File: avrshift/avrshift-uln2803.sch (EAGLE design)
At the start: 32 parts, among them IC1 AT90S2313P, IC2 7805TV

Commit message: some more minor adjustments (especially labels)
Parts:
- IC3, IC4: value (none) -> ULN2803A
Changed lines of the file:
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@@
 <part name="JP13" library="pinhead" deviceset="PINHD-1X2" device=""/>
 <part name="JP14" library="pinhead" deviceset="PINHD-1X2" device=""/>
-<part name="IC3" library="uln-udn" deviceset="ULN2803A" device=""/>
+<part name="IC3" library="uln-udn" deviceset="ULN2803A" device="" value="ULN2803A"/>
 <part name="JP2" library="pinhead" deviceset="PINHD-1X2" device=""/>
 <part name="JP3" library="pinhead" deviceset="PINHD-1X2" device=""/>
@@
 <part name="JP8" library="pinhead" deviceset="PINHD-1X2" device=""/>
 <part name="JP9" library="pinhead" deviceset="PINHD-1X2" device=""/>
-<part name="IC4" library="uln-udn" deviceset="ULN2803A" device=""/>
+<part name="IC4" library="uln-udn" deviceset="ULN2803A" device="" value="ULN2803A"/>
 </parts>
 <sheets>

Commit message: 😺
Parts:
- C2: device capacitor-wima:C2,5-3 -> rcl:C-EU050-024X044
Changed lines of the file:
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@@
 <part name="R2" library="rcl" deviceset="R-EU_" device="0207/2V" value="1K"/>
 <part name="C1" library="capacitor-wima" deviceset="C" device="2,5-3" value="330nF"/>
-<part name="C2" library="capacitor-wima" deviceset="C" device="2,5-3" value="100nF"/>
+<part name="C2" library="rcl" deviceset="C-EU" device="050-024X044" value="100nF"/>
 <part name="SJ1" library="jumper" deviceset="SJ" device="" value="BUSPWR"/>
 <part name="SV1" library="con-harting-ml" deviceset="ML10" device="" value="SI2C"/>

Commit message: avrshift-uln2803: start work on rev 2.1
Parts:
- added SV2: (no value), pinhead:PINHD-2X3
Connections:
- removed net N$3: IC1.RESET, R3.2
- new net RST: IC1.RESET, R3.1, SV2.5
- net 5V: now also R3.2, SV2.2; no longer R3.1
- net AVRO11: now also SV2.4
- net AVRO12: now also SV2.1
- net AVRO13: now also SV2.3
- net GND: now also SV2.6
- net N$10: now also R15.2; no longer R15.1
- net N$21: now also R18.1; no longer R18.2
- net N$33: now also R15.1; no longer R15.2
- net N$8: now also R18.2; no longer R18.1
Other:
- moved on the sheet: R15, R18, R3
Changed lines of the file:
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@@
 <part name="JP9" library="pinhead" deviceset="PINHD-1X2" device=""/>
 <part name="IC4" library="uln-udn" deviceset="ULN2803A" device="" value="ULN2803A"/>
+<part name="SV2" library="pinhead" deviceset="PINHD-2X3" device=""/>
 </parts>
 <sheets>
@@
 <instance part="SV1" gate="G$1" x="-53.34" y="50.8" rot="R180"/>
 <instance part="SJ2" gate="1" x="-25.4" y="71.12" rot="R270"/>
-<instance part="R3" gate="G$1" x="-38.1" y="7.62" rot="R90"/>
-<instance part="R15" gate="G$1" x="-48.26" y="17.78" rot="R90"/>
-<instance part="R18" gate="G$1" x="-58.42" y="17.78" rot="R90"/>
+<instance part="R3" gate="G$1" x="-38.1" y="7.62" rot="R270"/>
+<instance part="R15" gate="G$1" x="-48.26" y="20.32" rot="R270"/>
+<instance part="R18" gate="G$1" x="-58.42" y="20.32" rot="R270"/>
 <instance part="LED1" gate="G$1" x="-48.26" y="10.16"/>
 <instance part="LED2" gate="G$1" x="-58.42" y="10.16"/>
@@
 <instance part="JP9" gate="G$1" x="101.6" y="20.32"/>
 <instance part="IC4" gate="G$1" x="63.5" y="22.86"/>
+<instance part="SV2" gate="A" x="-12.7" y="-43.18"/>
 </instances>
 <busses>
@@
 <wire x1="45.72" y1="12.7" x2="45.72" y2="43.18" width="0.1524" layer="91"/>
 <junction x="45.72" y="43.18"/>
+</segment>
+<segment>
+<pinref part="SV2" gate="A" pin="6"/>
+<wire x1="-7.62" y1="-45.72" x2="7.62" y2="-45.72" width="0.1524" layer="91"/>
+<label x="-2.54" y="-45.72" size="1.778" layer="95"/>
 </segment>
 </net>
@@
 <segment>
 <pinref part="IC1" gate="G$1" pin="VCC"/>
+<label x="-66.04" y="0" size="1.778" layer="95"/>
 <wire x1="-30.48" y1="0" x2="-38.1" y2="0" width="0.1524" layer="91"/>
-<label x="-66.04" y="0" size="1.778" layer="95"/>
-<pinref part="R3" gate="G$1" pin="1"/>
+<pinref part="R3" gate="G$1" pin="2"/>
 <wire x1="-38.1" y1="0" x2="-68.58" y2="0" width="0.1524" layer="91"/>
 <wire x1="-38.1" y1="2.54" x2="-38.1" y2="0" width="0.1524" layer="91"/>
 <junction x="-38.1" y="0"/>
+</segment>
+<segment>
+<pinref part="SV2" gate="A" pin="2"/>
+<wire x1="-7.62" y1="-40.64" x2="7.62" y2="-40.64" width="0.1524" layer="91"/>
+<label x="-2.54" y="-40.64" size="1.778" layer="95"/>
 </segment>
 </net>
@@
 </segment>
 </net>
-<net name="N$3" class="0">
+<net name="RST" class="0">
 <segment>
 <pinref part="IC1" gate="G$1" pin="RESET"/>
 <wire x1="-30.48" y1="17.78" x2="-38.1" y2="17.78" width="0.1524" layer="91"/>
-<pinref part="R3" gate="G$1" pin="2"/>
+<pinref part="R3" gate="G$1" pin="1"/>
 <wire x1="-38.1" y1="17.78" x2="-38.1" y2="12.7" width="0.1524" layer="91"/>
 </segment>
-</net>
-<net name="N$8" class="0">
-<segment>
-<pinref part="R18" gate="G$1" pin="1"/>
-<pinref part="LED2" gate="G$1" pin="A"/>
-</segment>
-</net>
-<net name="N$10" class="0">
-<segment>
-<pinref part="R15" gate="G$1" pin="1"/>
-<pinref part="LED1" gate="G$1" pin="A"/>
+<segment>
+<pinref part="SV2" gate="A" pin="5"/>
+<wire x1="-15.24" y1="-45.72" x2="-27.94" y2="-45.72" width="0.1524" layer="91"/>
+<label x="-27.94" y="-45.72" size="1.778" layer="95"/>
 </segment>
 </net>
@@
 <wire x1="-33.02" y1="10.16" x2="-33.02" y2="27.94" width="0.1524" layer="91"/>
 <wire x1="-33.02" y1="27.94" x2="-58.42" y2="27.94" width="0.1524" layer="91"/>
-<pinref part="R18" gate="G$1" pin="2"/>
-<wire x1="-58.42" y1="27.94" x2="-58.42" y2="22.86" width="0.1524" layer="91"/>
+<pinref part="R18" gate="G$1" pin="1"/>
+<wire x1="-58.42" y1="25.4" x2="-58.42" y2="27.94" width="0.1524" layer="91"/>
 </segment>
 </net>
@@
 <wire x1="-35.56" y1="5.08" x2="-35.56" y2="25.4" width="0.1524" layer="91"/>
 <wire x1="-35.56" y1="25.4" x2="-48.26" y2="25.4" width="0.1524" layer="91"/>
-<pinref part="R15" gate="G$1" pin="2"/>
-<wire x1="-48.26" y1="25.4" x2="-48.26" y2="22.86" width="0.1524" layer="91"/>
+<pinref part="R15" gate="G$1" pin="1"/>
 </segment>
 </net>
@@
 <label x="35.56" y="53.34" size="1.778" layer="95"/>
 </segment>
+<segment>
+<pinref part="SV2" gate="A" pin="4"/>
+<wire x1="-7.62" y1="-43.18" x2="7.62" y2="-43.18" width="0.1524" layer="91"/>
+<label x="-2.54" y="-43.18" size="1.778" layer="95"/>
+</segment>
 </net>
 <net name="AVRO12" class="0">
@@
 <label x="35.56" y="55.88" size="1.778" layer="95"/>
 </segment>
+<segment>
+<pinref part="SV2" gate="A" pin="1"/>
+<wire x1="-15.24" y1="-40.64" x2="-27.94" y2="-40.64" width="0.1524" layer="91"/>
+<label x="-27.94" y="-40.64" size="1.778" layer="95"/>
+</segment>
 </net>
 <net name="AVRO13" class="0">
@@
 <wire x1="50.8" y1="58.42" x2="35.56" y2="58.42" width="0.1524" layer="91"/>
 <label x="35.56" y="58.42" size="1.778" layer="95"/>
+</segment>
+<segment>
+<pinref part="SV2" gate="A" pin="3"/>
+<wire x1="-15.24" y1="-43.18" x2="-27.94" y2="-43.18" width="0.1524" layer="91"/>
+<label x="-27.94" y="-43.18" size="1.778" layer="95"/>
 </segment>
 </net>
@@
 </segment>
 </net>
+<net name="N$8" class="0">
+<segment>
+<pinref part="R18" gate="G$1" pin="2"/>
+<pinref part="LED2" gate="G$1" pin="A"/>
+<wire x1="-58.42" y1="15.24" x2="-58.42" y2="12.7" width="0.1524" layer="91"/>
+</segment>
+</net>
+<net name="N$10" class="0">
+<segment>
+<pinref part="R15" gate="G$1" pin="2"/>
+<pinref part="LED1" gate="G$1" pin="A"/>
+<wire x1="-48.26" y1="15.24" x2="-48.26" y2="12.7" width="0.1524" layer="91"/>
+</segment>
+</net>

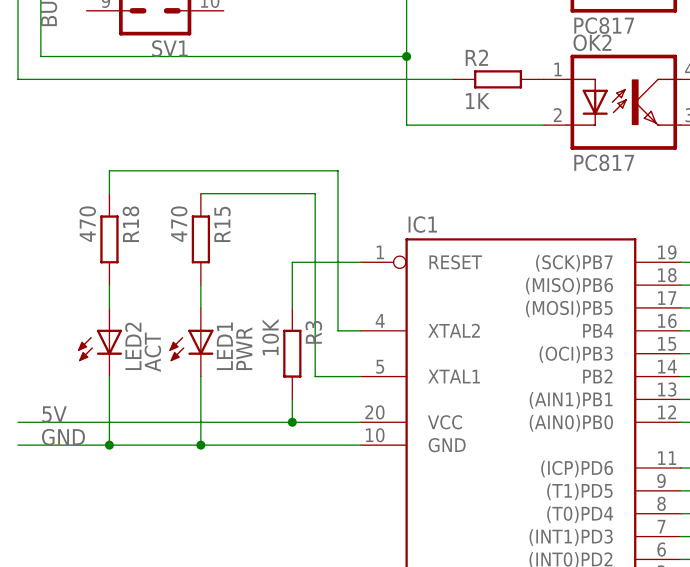
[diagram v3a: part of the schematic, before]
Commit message: avrshift: Add labels for avrmf pins, extend VCC net to 7805 and input
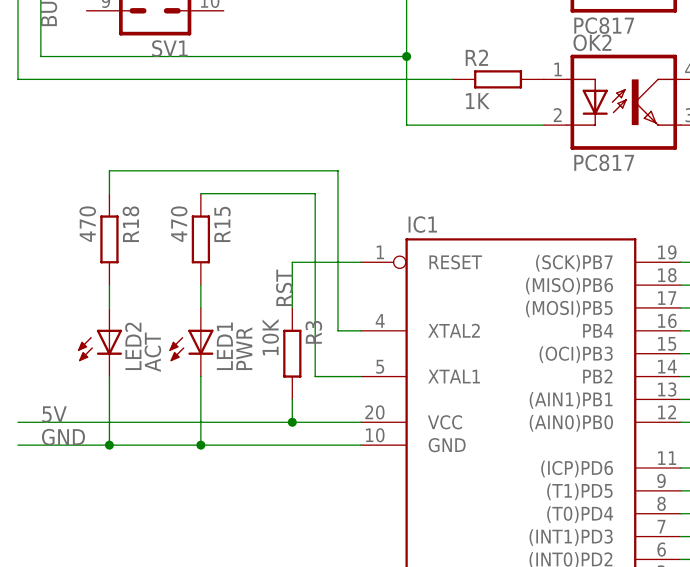
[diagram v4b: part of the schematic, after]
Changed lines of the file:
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@@
 <pinref part="R3" gate="G$1" pin="1"/>
 <wire x1="-38.1" y1="17.78" x2="-38.1" y2="12.7" width="0.1524" layer="91"/>
+<label x="-38.1" y="12.7" size="1.778" layer="95" rot="R90"/>
 </segment>
 <segment>

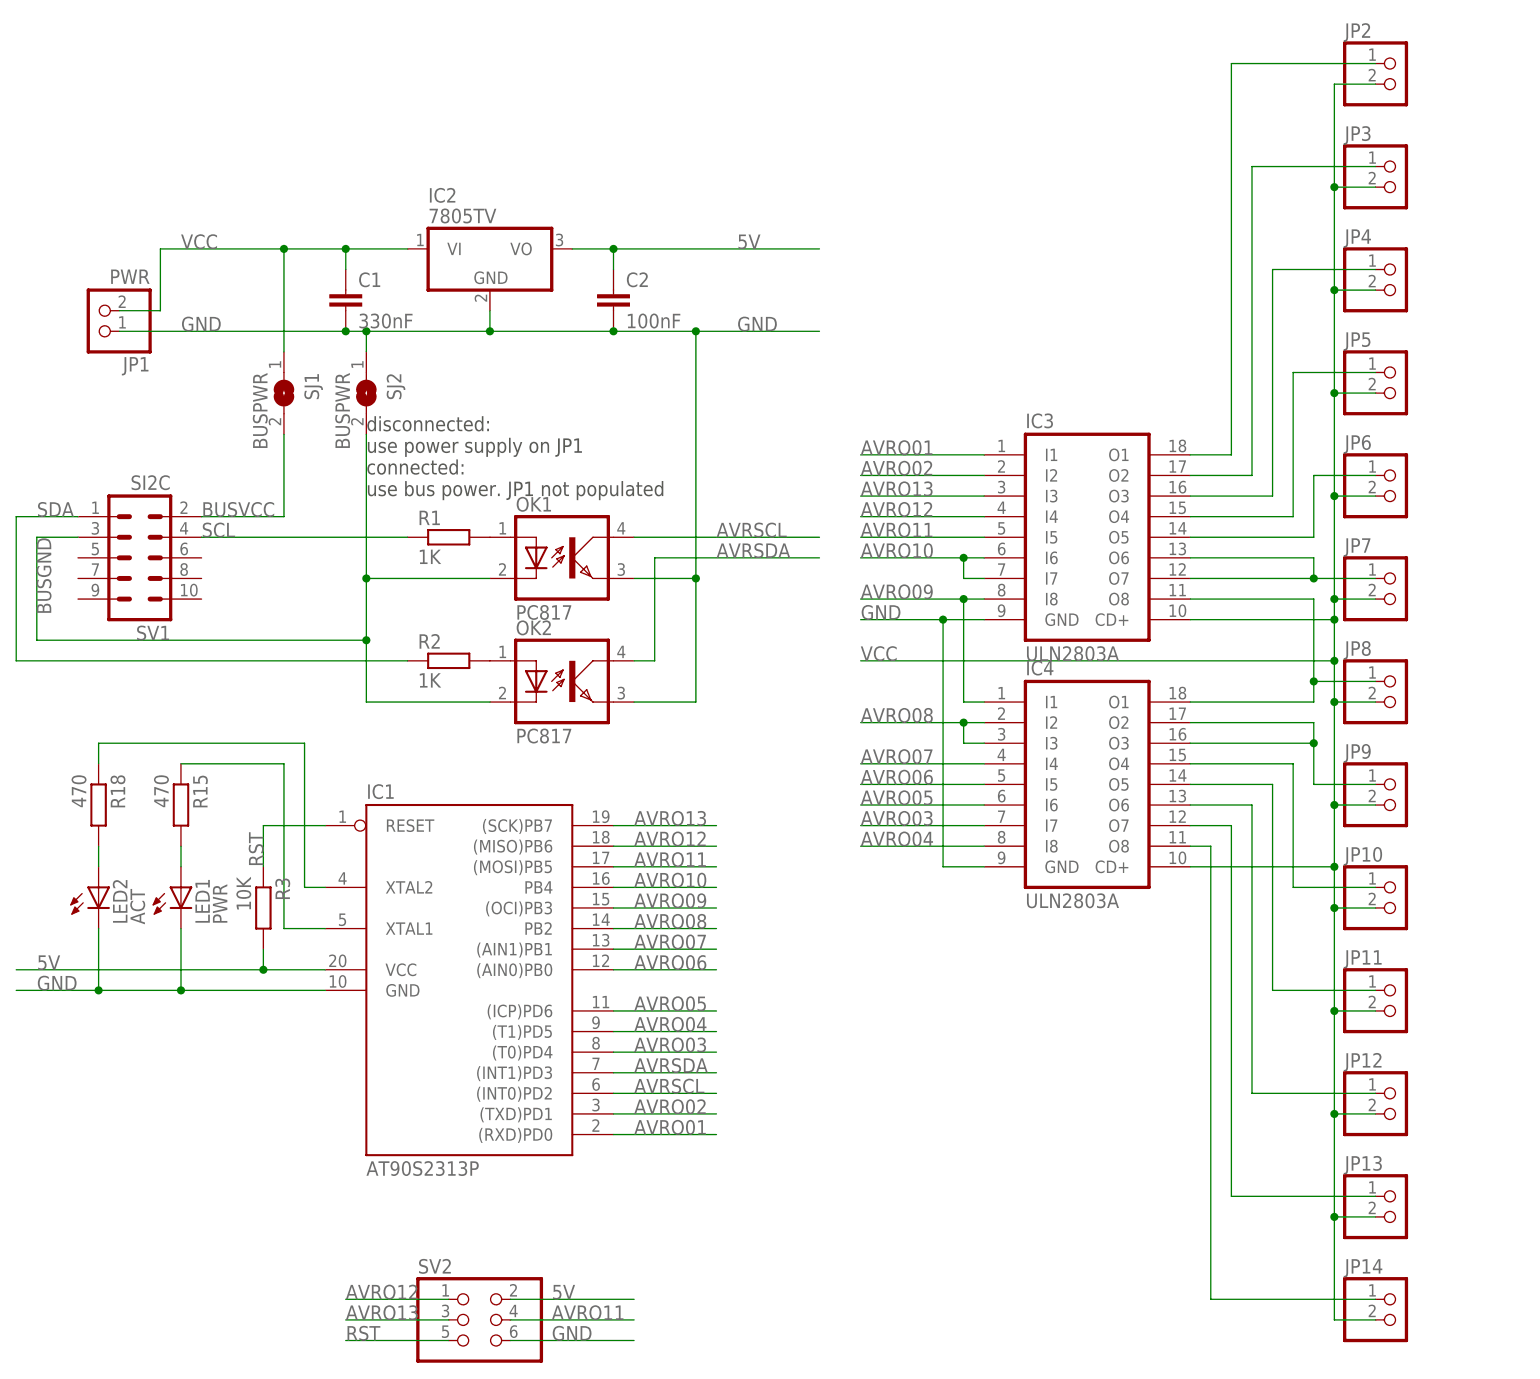
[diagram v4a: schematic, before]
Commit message: avrshift-uln2803: switch to (cheaper) SMD ATTiny
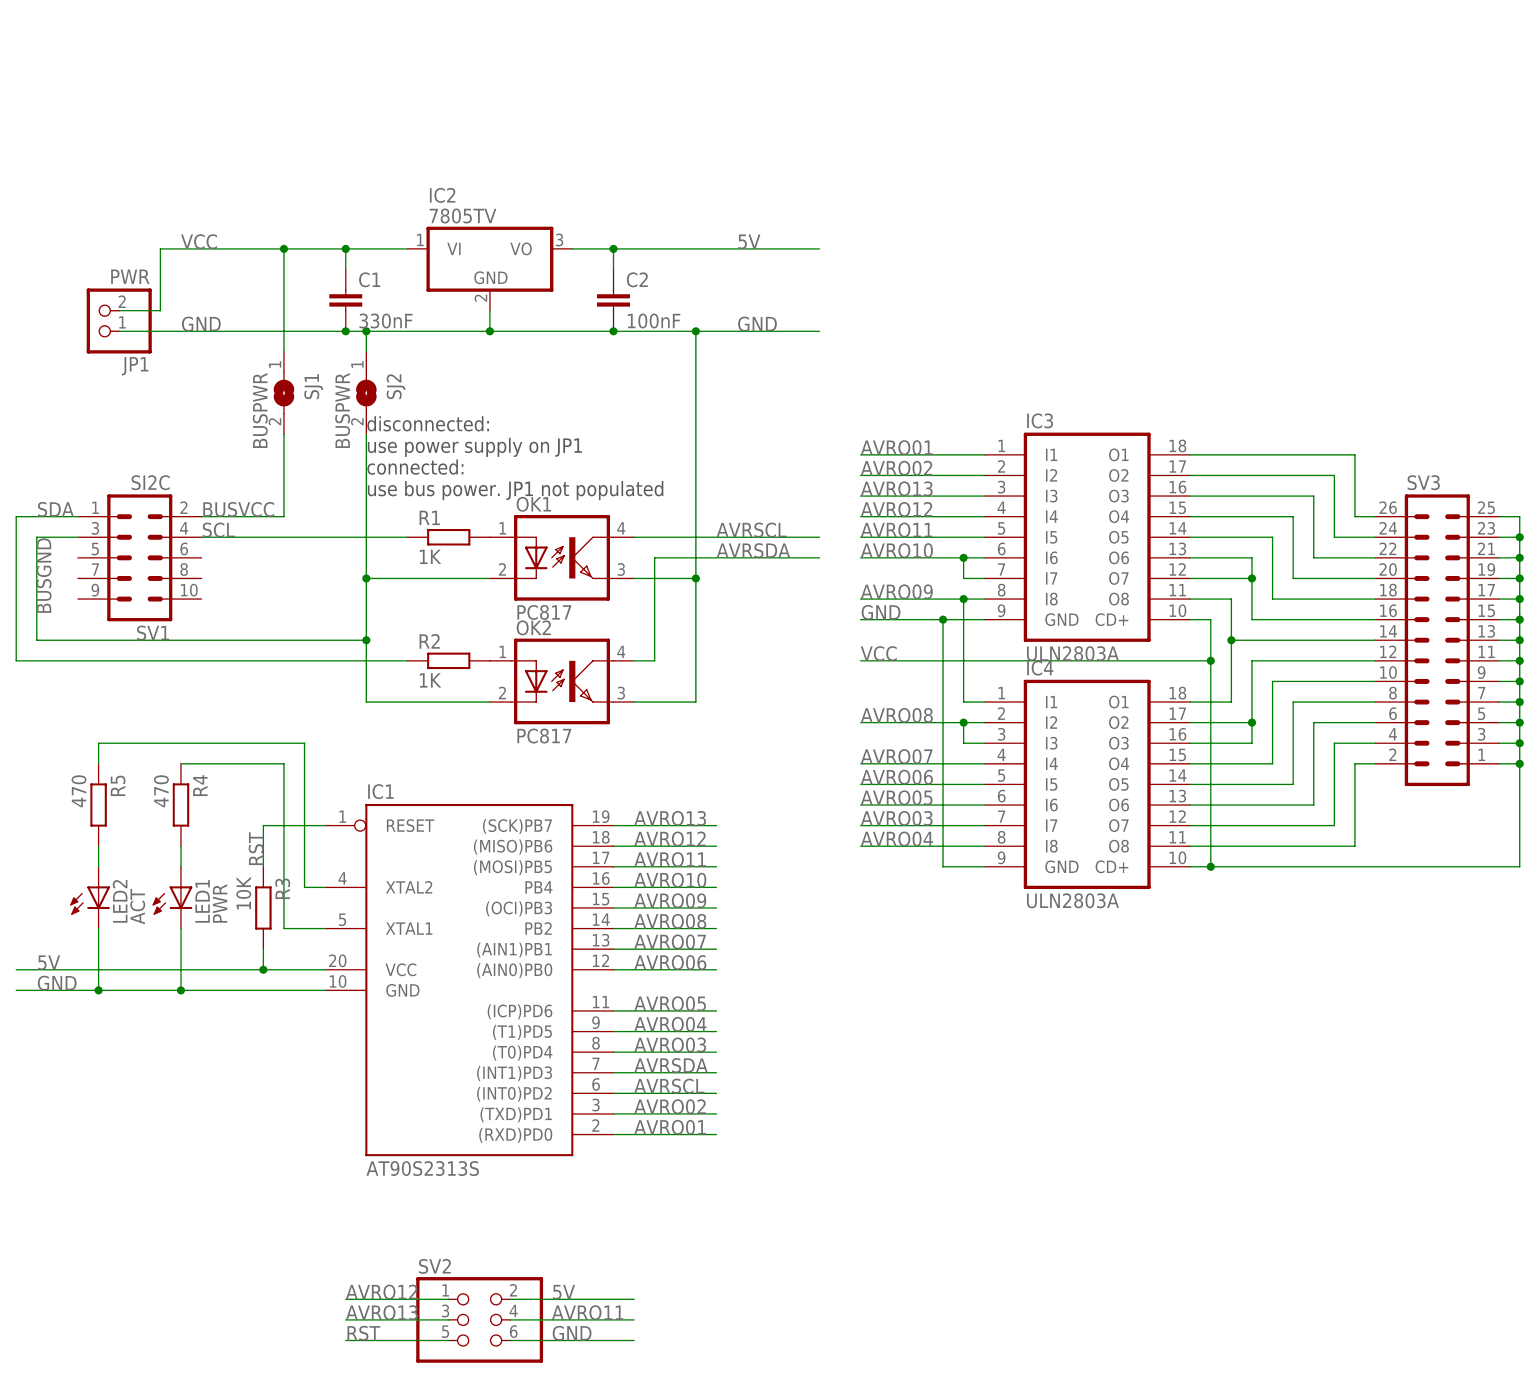
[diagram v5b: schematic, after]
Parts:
- removed JP10, JP11, JP12, JP13, JP14, JP2, JP3, JP4, JP5, JP6, JP7, JP8, JP9: (no value), pinhead:PINHD-1X2
- removed R15, R18: 470, rcl:R-EU_0207/2V
- added R4, R5: 470, rcl:R-EU_R0805
- added SV3: (no value), con-ml:ML26
- C2: device rcl:C-EU050-024X044 -> rcl:C-EUC0805
- IC1: value AT90S2313P -> AT90S2313S; device atmel:AT90S2313P -> atmel:AT90S2313S
- LED1, LED2: device led:LED3MM -> led:LEDSML0805
- R1, R2, R3: device rcl:R-EU_0207/2V -> rcl:R-EU_R0805
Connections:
- net N$10: now also R4.2; no longer R15.2
- net N$11: now also SV3.10; no longer JP10.1
- net N$12: now also SV3.12; no longer JP9.1
- net N$13: now also SV3.14; no longer JP8.1
- net N$14: now also SV3.16; no longer JP7.1
- net N$15: now also SV3.18; no longer JP6.1
- net N$17: now also SV3.4; no longer JP13.1
- net N$18: now also SV3.2; no longer JP14.1
- net N$2: now also SV3.26; no longer JP2.1
- net N$21: now also R5.1; no longer R18.1
- net N$25: now also SV3.20; no longer JP5.1
- net N$33: now also R4.1; no longer R15.1
- net N$5: now also SV3.24; no longer JP3.1
- net N$6: now also SV3.22; no longer JP4.1
- net N$7: now also SV3.8; no longer JP11.1
- net N$8: now also R5.2; no longer R18.2
- net N$9: now also SV3.6; no longer JP12.1
- net VCC: now also SV3.1, SV3.11, SV3.13, SV3.15, SV3.17, SV3.19, SV3.21, SV3.23, SV3.25, SV3.3, SV3.5, SV3.7, SV3.9; no longer JP10.2, JP11.2, JP12.2, JP13.2, JP14.2, JP2.2, JP3.2, JP4.2, JP5.2, JP6.2, JP7.2, JP8.2, JP9.2
